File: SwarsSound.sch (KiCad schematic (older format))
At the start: 162 parts, among them P1 Main_Connector, P2 aud_con, P3 edge_con, Q1 2N3906f, Q2 2N3906f, Q3 2N3904, Q4 2N3904

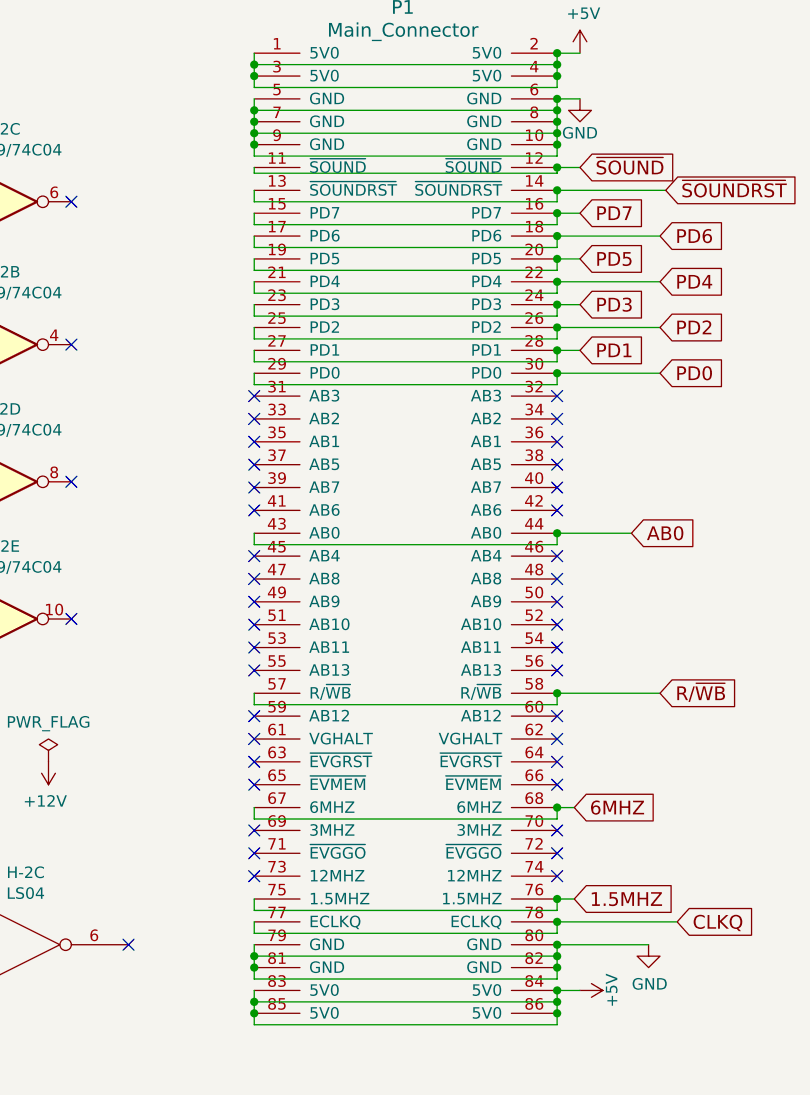
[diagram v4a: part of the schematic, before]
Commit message: Added top layer
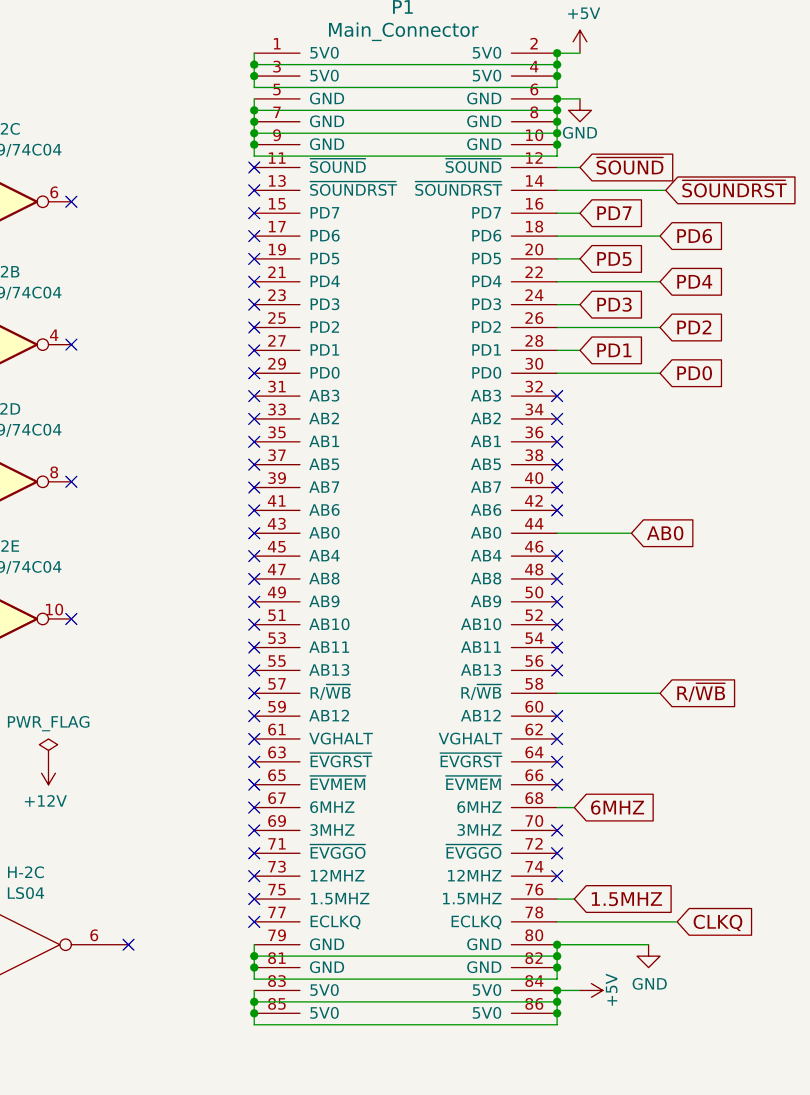
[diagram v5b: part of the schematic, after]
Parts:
- D-2, D-3, D-4, D-5, E-1: footprint Package_DIP:DIP-40_W15.24mm -> Star_Wars_Vector_PCB:DDIP40
- F-2, F/H-5, H-2: footprint (none) -> Star_Wars_Vector_PCB:DIP14
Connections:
- net 1.5MHZ: no longer P1.75 (1.5MHZ)
- net 6MHZ: no longer P1.67 (6MHZ)
- net AB0: no longer P1.43 (AB0)
- net CLKQ: no longer P1.77 (ECLKQ)
- net PD0: no longer P1.29 (PD0)
- net PD1: no longer P1.27 (PD1)
- net PD2: no longer P1.25 (PD2)
- net PD3: no longer P1.23 (PD3)
- net PD4: no longer P1.21 (PD4)
- net PD5: no longer P1.19 (PD5)
- net PD6: no longer P1.17 (PD6)
- net PD7: no longer P1.15 (PD7)
- net R/~WB: no longer P1.57 (R/~WB)
- net ~SOUND: no longer P1.11 (~SOUND)
- net ~SOUNDRST: no longer P1.13 (~SOUNDRST)
- no-connect marks 107 -> 122
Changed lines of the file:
@@
 Connection ~ 31325 21050
 Wire Wire Line
-	30000 20800 30000 20850
-Wire Wire Line
-	30000 20850 31325 20850
-Wire Wire Line
-	31325 20850 31325 20800
-Wire Wire Line
-	30000 20400 30000 20450
-Wire Wire Line
-	30000 20450 31325 20450
-Wire Wire Line
-	31325 20450 31325 20400
-Wire Wire Line
-	30000 19950 31325 19950
-Wire Wire Line
-	31325 19950 31325 19900
-Wire Wire Line
-	30000 17800 30000 17850
-Wire Wire Line
-	30000 17850 31325 17850
-Wire Wire Line
-	31325 17850 31325 17800
-Wire Wire Line
-	30000 17900 30000 17950
-Wire Wire Line
-	30000 17950 31325 17950
-Wire Wire Line
-	31325 17950 31325 17900
-Wire Wire Line
-	30000 18000 30000 18050
-Wire Wire Line
-	30000 18050 31325 18050
-Wire Wire Line
-	31325 18050 31325 18000
-Wire Wire Line
-	30000 18100 30000 18150
-Wire Wire Line
-	30000 18150 31325 18150
-Wire Wire Line
-	31325 18150 31325 18100
-Wire Wire Line
-	30000 18200 30000 18250
-Wire Wire Line
-	30000 18250 31325 18250
-Wire Wire Line
-	31325 18250 31325 18200
-Wire Wire Line
-	30000 18300 30000 18350
-Wire Wire Line
-	30000 18350 31325 18350
-Wire Wire Line
-	31325 18350 31325 18300
-Wire Wire Line
-	30000 18400 30000 18450
-Wire Wire Line
-	30000 18450 31325 18450
-Wire Wire Line
-	31325 18450 31325 18400
-Wire Wire Line
-	30000 18500 30000 18550
-Wire Wire Line
-	30000 18550 31325 18550
-Wire Wire Line
-	31325 18550 31325 18500
-Wire Wire Line
 	31425 17300 31325 17300
 Wire Wire Line
@@
 	31325 17400 31325 17450
 Connection ~ 31325 17400
-Connection ~ 31325 20800
 Wire Wire Line
 	30000 17350 30000 17400
@@
 	30000 17400 30000 17450
 Connection ~ 30000 17400
-Connection ~ 31325 20400
 Connection ~ 31325 17300
-Connection ~ 31325 19900
 Wire Wire Line
 	31325 17200 31325 17250
@@
 	31325 17150 31325 17200
 Connection ~ 31325 17200
-Connection ~ 31325 18500
 Wire Wire Line
 	30000 17150 30000 17200
@@
 	30000 17200 30000 17250
 Connection ~ 30000 17200
-Connection ~ 31325 18400
-Connection ~ 31325 18300
-Connection ~ 31325 18200
-Connection ~ 31325 18100
-Connection ~ 31325 18000
 Connection ~ 31325 17100
-Connection ~ 31325 17900
-Connection ~ 31325 17800
 Wire Wire Line
 	31325 17450 31325 17500
@@
 NoConn ~ 30000 19400
 NoConn ~ 30000 19300
-Wire Wire Line
-	30000 19900 30000 19950
 NoConn ~ 30000 20000
 NoConn ~ 30000 20100
@@
 	31850 20900 31325 20900
 Wire Wire Line
-	31325 20900 31325 20950
-Wire Wire Line
-	31325 20950 30000 20950
-Wire Wire Line
-	30000 20950 30000 20900
-Connection ~ 31325 20900
-Wire Wire Line
-	31325 19250 30000 19250
-Wire Wire Line
-	30000 19250 30000 19200
-Wire Wire Line
-	31325 19200 31325 19250
-Wire Wire Line
 	31650 19200 31325 19200
-Connection ~ 31325 19200
 Wire Wire Line
 	31425 17600 31325 17600
 Wire Wire Line
-	31325 17600 31325 17625
-Wire Wire Line
-	31325 17625 30000 17625
-Wire Wire Line
-	30000 17625 30000 17600
-Connection ~ 31325 17600
-Wire Wire Line
 	31800 17700 31325 17700
-Wire Wire Line
-	31325 17700 31325 17750
-Wire Wire Line
-	31325 17750 30000 17750
-Wire Wire Line
-	30000 17750 30000 17700
-Connection ~ 31325 17700
 Text GLabel 7750 17175 0    60   Input ~ 0
 P
@@
 F 0 "E-1" H 26725 4875 50  0000 C CNN
 F 1 "6532A PIA" H 27150 3475 50  0000 C CNN
-F 2 "Package_DIP:DIP-40_W15.24mm" H 27500 2050 50  0001 L CNN
+F 2 "Star_Wars_Vector_PCB:DDIP40" H 27500 2050 50  0001 L CNN
 F 3 "" H 27150 3400 50  0001 C CNN
 	1    27150 3400
@@
 F 0 "D-5" H 1900 13425 50  0000 C CNN
 F 1 "CI/O 0" H 2300 12400 50  0000 C CNN
-F 2 "Package_DIP:DIP-40_W15.24mm" H 2650 11175 50  0001 L CNN
+F 2 "Star_Wars_Vector_PCB:DDIP40" H 2650 11175 50  0001 L CNN
 F 3 "" H 2300 12525 50  0001 C CNN
 	1    2300 12525
@@
 F 0 "D-4" H 3900 13425 50  0000 C CNN
 F 1 "CI/O 1" H 4300 12400 50  0000 C CNN
-F 2 "Package_DIP:DIP-40_W15.24mm" H 4650 11175 50  0001 L CNN
+F 2 "Star_Wars_Vector_PCB:DDIP40" H 4650 11175 50  0001 L CNN
 F 3 "" H 4300 12525 50  0001 C CNN
 	1    4300 12525
@@
 F 0 "D-3" H 5900 13425 50  0000 C CNN
 F 1 "CI/O 2" H 6300 12400 50  0000 C CNN
-F 2 "Package_DIP:DIP-40_W15.24mm" H 6650 11175 50  0001 L CNN
+F 2 "Star_Wars_Vector_PCB:DDIP40" H 6650 11175 50  0001 L CNN
 F 3 "" H 6300 12525 50  0001 C CNN
 	1    6300 12525
@@
 F 0 "D-2" H 7900 13425 50  0000 C CNN
 F 1 "CI/O 3" H 8300 12400 50  0000 C CNN
-F 2 "Package_DIP:DIP-40_W15.24mm" H 8650 11175 50  0001 L CNN
+F 2 "Star_Wars_Vector_PCB:DDIP40" H 8650 11175 50  0001 L CNN
 F 3 "" H 8300 12525 50  0001 C CNN
 	1    8300 12525
@@
 F 0 "H-2" H 29000 21315 50  0000 C CNN
 F 1 "LS04" H 29000 21224 50  0000 C CNN
-F 2 "" H 29000 21000 50  0001 C CNN
+F 2 "Star_Wars_Vector_PCB:DIP14" H 29000 21000 50  0001 C CNN
 F 3 "" H 29000 21000 50  0001 C CNN
 	3    29000 21000
@@
 F 0 "F-2" H 28900 19892 50  0000 C CNN
 F 1 "CD4069/74C04" H 28900 19801 50  0000 C CNN
-F 2 "" H 28900 19575 50  0001 C CNN
+F 2 "Star_Wars_Vector_PCB:DIP14" H 28900 19575 50  0001 C CNN
 F 3 "" H 28900 19575 50  0001 C CNN
 	5    28900 19575
@@
 F 0 "F-2" H 28900 19292 50  0000 C CNN
 F 1 "CD4069/74C04" H 28900 19201 50  0000 C CNN
-F 2 "" H 28900 18975 50  0001 C CNN
+F 2 "Star_Wars_Vector_PCB:DIP14" H 28900 18975 50  0001 C CNN
 F 3 "" H 28900 18975 50  0001 C CNN
 	4    28900 18975
@@
 F 0 "F-2" H 28900 18692 50  0000 C CNN
 F 1 "CD4069/74C04" H 28900 18601 50  0000 C CNN
-F 2 "" H 28900 18375 50  0001 C CNN
+F 2 "Star_Wars_Vector_PCB:DIP14" H 28900 18375 50  0001 C CNN
 F 3 "" H 28900 18375 50  0001 C CNN
 	2    28900 18375
@@
 F 0 "F/H-5" H 27700 20517 50  0000 C CNN
 F 1 "74LS125" H 27700 20426 50  0000 C CNN
-F 2 "" H 27700 20200 50  0001 C CNN
+F 2 "Star_Wars_Vector_PCB:DIP14" H 27700 20200 50  0001 C CNN
 F 3 "http://www.ti.com/lit/gpn/sn74LS125" H 27700 20200 50  0001 C CNN
 	4    27700 20200
@@
 F 0 "F-2" H 28900 18067 50  0000 C CNN
 F 1 "CD4069/74C04" H 28900 17976 50  0000 C CNN
-F 2 "" H 28900 17750 50  0001 C CNN
+F 2 "Star_Wars_Vector_PCB:DIP14" H 28900 17750 50  0001 C CNN
 F 3 "" H 28900 17750 50  0001 C CNN
 	3    28900 17750
@@
 $EndComp
 $Comp
-L power:GND #PWR?
+L power:GND #PWR0259
 U 1 1 613014FD
 P 28600 17750
-F 0 "#PWR?" H 28600 17500 50  0001 C CNN
+F 0 "#PWR0259" H 28600 17500 50  0001 C CNN
 F 1 "GND" H 28605 17577 50  0000 C CNN
 F 2 "" H 28600 17750 50  0001 C CNN
@@
 $EndComp
 NoConn ~ 29200 17750
+NoConn ~ 30000 20400
+NoConn ~ 30000 17600
+NoConn ~ 30000 17700
+NoConn ~ 30000 17800
+NoConn ~ 30000 17900
+NoConn ~ 30000 18000
+NoConn ~ 30000 18100
+NoConn ~ 30000 18200
+NoConn ~ 30000 18300
+NoConn ~ 30000 18400
+NoConn ~ 30000 18500
+NoConn ~ 30000 19200
+NoConn ~ 30000 19900
+NoConn ~ 30000 20800
+NoConn ~ 30000 20900
 $EndSCHEMATC

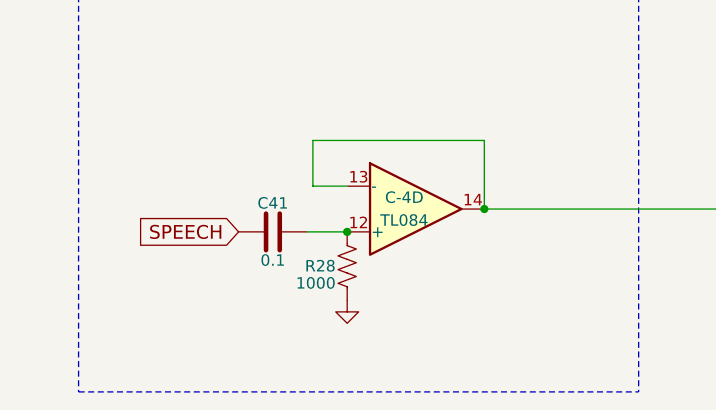
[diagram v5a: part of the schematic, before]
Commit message: Changed R28 value from 1k to 100k in schematic and BOM
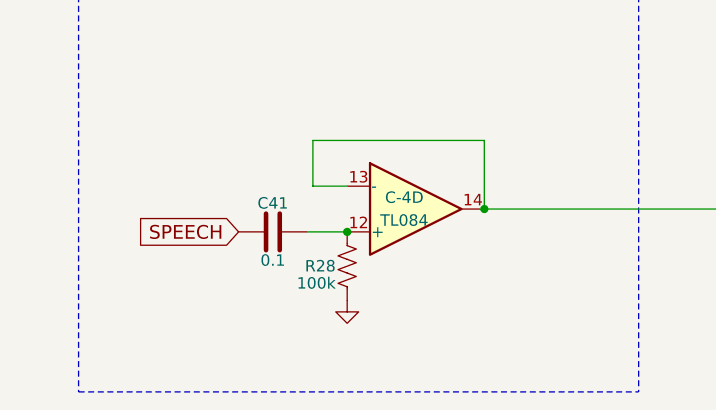
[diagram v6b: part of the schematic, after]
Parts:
- R28: value 1000 -> 100k
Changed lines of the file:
@@
 P 2175 21825
 F 0 "R28" H 2225 21825 50  0000 L CNN
-F 1 "1000" H 2225 21900 50  0000 L CNN
+F 1 "100k" H 2225 21900 50  0000 L CNN
 F 2 "Star_Wars_Vector_PCB:GenericComp" V 2215 21815 50  0001 C CNN
 F 3 "~" H 2175 21825 50  0001 C CNN
